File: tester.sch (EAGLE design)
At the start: 73 parts, among them IC1 ATmega8/88/168, K1 NA 05W K, M1 SP6000C-180, P1 250, P2 10k lin, Q1 BC847CSMD, Q2 BC847CSMD, Q3 BC807-40SMD, Q4 8,000 MHz, Q5 BC847CSMD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

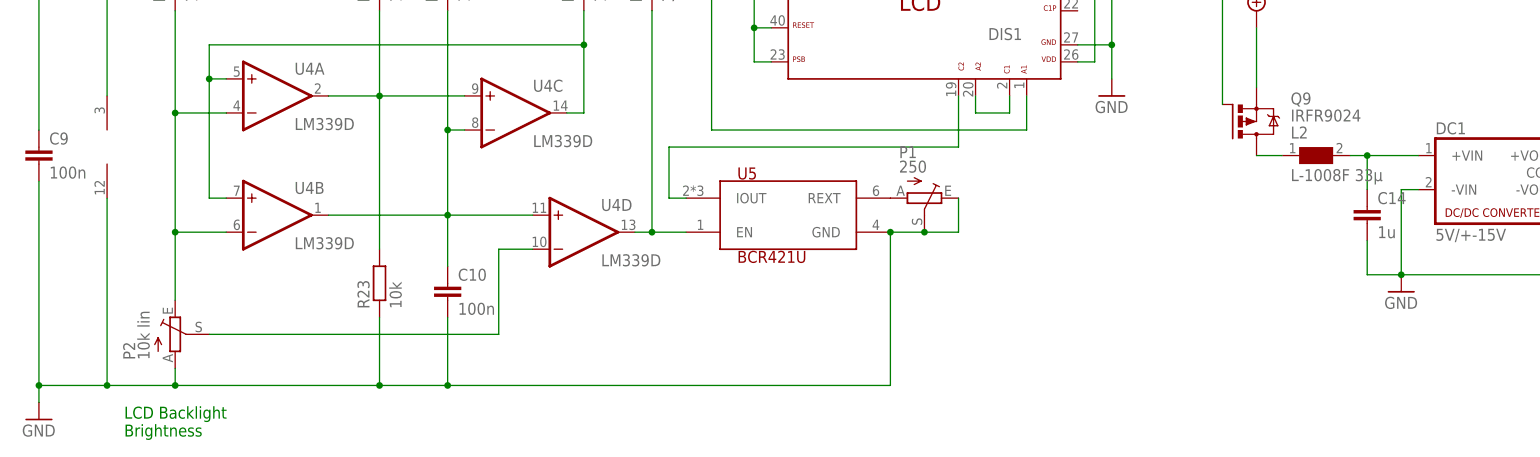
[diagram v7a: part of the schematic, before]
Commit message: changed all r/c to 0805, resized some pads, hopefully made easier to solder
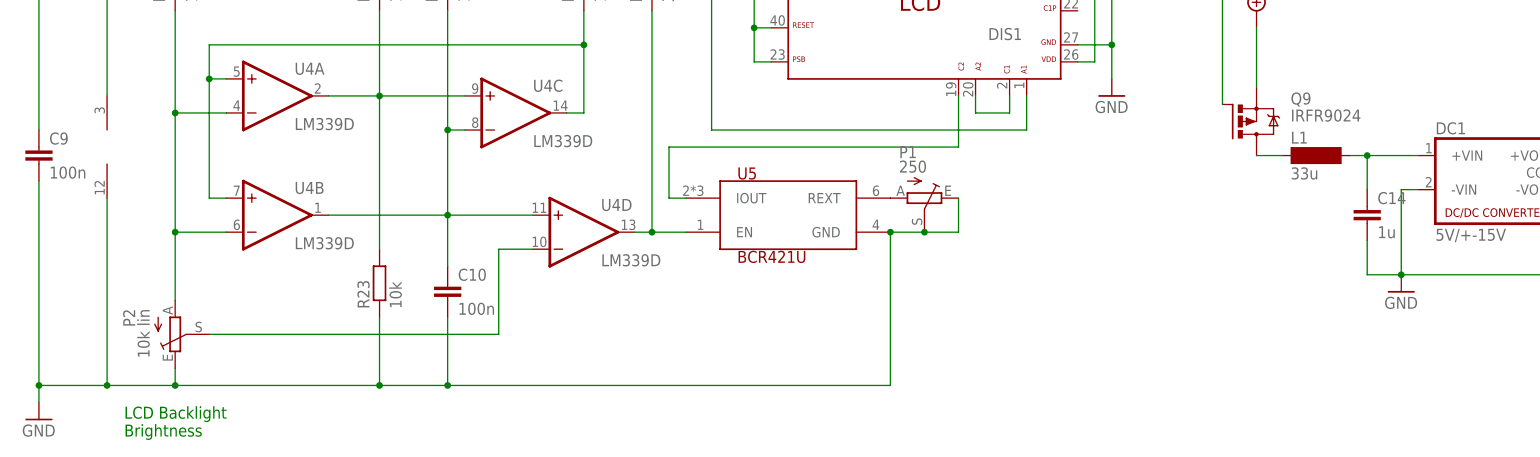
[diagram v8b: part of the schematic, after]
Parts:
- removed L2: L-1008F 33µ, EagleLibrary_Wuerth_Elektronik_eiSos_Version_6:WE-RFI_1008
- added L1: 33u, inductor-neosid:SM-NE29
- C1, C10, C3, C4, C9: device resistor:C-EUC0603 -> resistor:C-EUC0805
- C11, C12, C13, C14, C17, C2, C6, C7, C8: device rcl:C-EUC0603 -> rcl:C-EUC0805
- C15, C5: device rcl:CPOL-EUUD-5X5,8 -> rcl:CPOL-EU153CLV-0505
- D3: device markus:SCHOTTKY-DIODE_RAD3-5-A -> markus:SCHOTTKY-DIODE_3-10
- R10, R11, R12, R13, R14, R16, R17, R19, R20, R21, R22, R23, R24, R26, R7, R8, R9: device resistor:R-EU_R0603 -> resistor:R-EU_R0805
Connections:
- net GND: now also P2.E; no longer P2.A
- net N$15: now also P2.A; no longer P2.E
- net N$24: now also L1.1; no longer L2.1
- net N$25: now also L1.2; no longer L2.2
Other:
- moved on the sheet: P2
